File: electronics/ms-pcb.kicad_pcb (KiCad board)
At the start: 2 copper layers, 110 x 110 mm, 28 parts, among them J1 Left motor, J2 Right motor, J3 XT60-M, U1 ESP32-S3-DEVKITC-1U-N8R2, U2 GY-521

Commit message: elec: start PCB v1.1.0
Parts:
- added C1: 0.1uF, Capacitor_THT:CP_Radial_D5.0mm_P2.00mm, F.Cu at (108.7, 107.0)
- added C2: 0.1uF, Capacitor_THT:CP_Radial_D5.0mm_P2.00mm, F.Cu at (141.0, 106.7)
- added D1: D_Schottky, Diode_SMD:D_1206_3216Metric_Pad1.42x1.75mm_HandSolder, F.Cu at (148.8, 76.2)
- added D2: DEBUG, LED_SMD:LED_1206_3216Metric_Pad1.42x1.75mm_HandSolder, F.Cu at (87.4, 76.7)
- added R3: 10k, Resistor_SMD:R_1206_3216Metric_Pad1.30x1.75mm_HandSolder, F.Cu at (130.0, 65.0)
- added R4: 5k, Resistor_SMD:R_1206_3216Metric_Pad1.30x1.75mm_HandSolder, F.Cu at (97.8, 64.8)
- added R8: 1k, Resistor_SMD:R_1206_3216Metric_Pad1.30x1.75mm_HandSolder, F.Cu at (136.9, 65.0)
- D3: renamed from D1; value GREEN -> LED_VBAT
- D4: renamed from D2; value BLUE -> LED_3V3
- H5: renamed from H2; value Caster_wheel_holes -> Caster_wheel
- H6: renamed from H5; value Caster_wheel_holes -> Caster_wheel
- moved U1 2.93 mm to (123.6, 71.0), turned to 90 degrees
- moved D3 2.12 mm to (132.6, 103.8)
- moved R5 2.12 mm to (132.6, 98.8)
- renumbered H3 to H1, H6 to H2, H1 to H3, R3 to R5, R4 to R6, R5 to R7
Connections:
- R2 pad 2: Vmes -> Mes_bat
- R7 pad 1: Vmes -> Mes_bat
- S1 pad G1: Net-(S1-PadG1) -> unconnected-(S1-PadG1)_0
- S1 pad G2: Net-(S1-PadG1) -> unconnected-(S1-PadG1)
- U1 pad J1_10: unconnected-(U1-GPIO17-PadJ1_10) -> button
- U1 pad J1_13: unconnected-(U1-GPIO3-PadJ1_13) -> Mes_bat
- U1 pad J1_14: unconnected-(U1-GPIO46-PadJ1_14) -> DRV_L1
- U1 pad J1_15: unconnected-(U1-GPIO9-PadJ1_15) -> DRV_L2
- U1 pad J1_16: XSHUT_FR -> DRV_R2
- U1 pad J1_17: XSHUT_R -> DRV_R1
- U1 pad J1_19: XSHUT_L -> ENC_R1
- U1 pad J1_20: XSHUT_FL -> ENC_R2
- U1 pad J1_21: +BATT -> Net-(D1-K)
- U1 pad J1_4: SDA -> ENC_L1
- U1 pad J1_5: SCL -> ENC_L2
- U1 pad J1_6: unconnected-(U1-GPIO6-PadJ1_6) -> buzzer
- U1 pad J3_10: DRV_R1 -> unconnected-(U1-GPIO38-PadJ3_10)
- U1 pad J3_11: DRV_R2 -> unconnected-(U1-GPIO37-PadJ3_11)
- U1 pad J3_12: DRV_L2 -> unconnected-(U1-GPIO36-PadJ3_12)
- U1 pad J3_13: DRV_L1 -> unconnected-(U1-GPIO35-PadJ3_13)
- U1 pad J3_16: buzzer -> Mes_VCC
- U1 pad J3_17: button -> SDA
- U1 pad J3_18: ENC_L2 -> SCL
- U1 pad J3_19: Vmes -> XSHUT_FR
- U1 pad J3_20: ENC_L1 -> XSHUT_R
- U1 pad J3_4: unconnected-(U1-GPIO1-PadJ3_4) -> XSHUT_FL
- U1 pad J3_5: unconnected-(U1-GPIO2-PadJ3_5) -> DEBUG
- U1 pad J3_6: ENC_R2 -> unconnected-(U1-MTMS/GPIO42-PadJ3_6)
- U1 pad J3_7: ENC_R1 -> unconnected-(U1-MTDI/GPIO41-PadJ3_7)
- U1 pad J3_8: unconnected-(U1-MTDO/GPIO40-PadJ3_8) -> XSHUT_L
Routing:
- net +BATT: track 193.4 -> 84.4 mm
- net SDA: track 175.3 -> 112.4 mm
- net SCL: track 185.9 -> 123.9 mm
- net Vmes: track 59.5 -> 0.00 mm, vias 1 -> 0
- net XSHUT_R: track 44.0 -> 0.00 mm, vias 2 -> 0
- net XSHUT_FR: track 43.6 -> 0.00 mm, vias 2 -> 0
- net MOT_R2: track 40.2 -> 0.00 mm
- net MOT_R1: track 35.9 -> 0.07 mm
- net MOT_L2: track 34.3 -> 0.00 mm
- net XSHUT_FL: track 34.1 -> 0.00 mm
- net MOT_L1: track 33.3 -> 0.00 mm
- net ENC_L2: track 30.1 -> 3.90 mm
- net XSHUT_F: track 23.4 -> 0.00 mm
- net ENC_L1: track 26.9 -> 4.16 mm
- net +3.3V: track 31.5 -> 11.8 mm, vias 5 -> 3
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
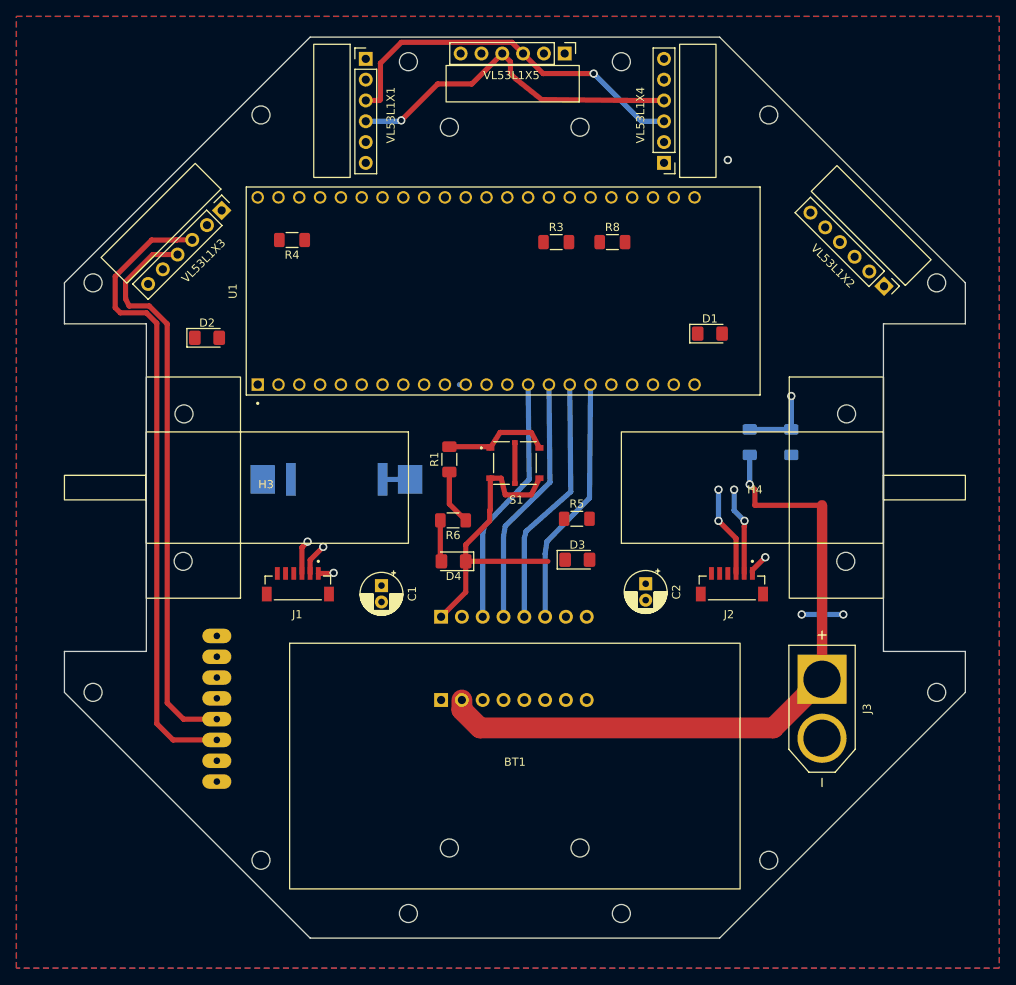
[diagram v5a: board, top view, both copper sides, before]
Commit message: elec: PCB v1.1.0 finished
Still need last checks before ordering.
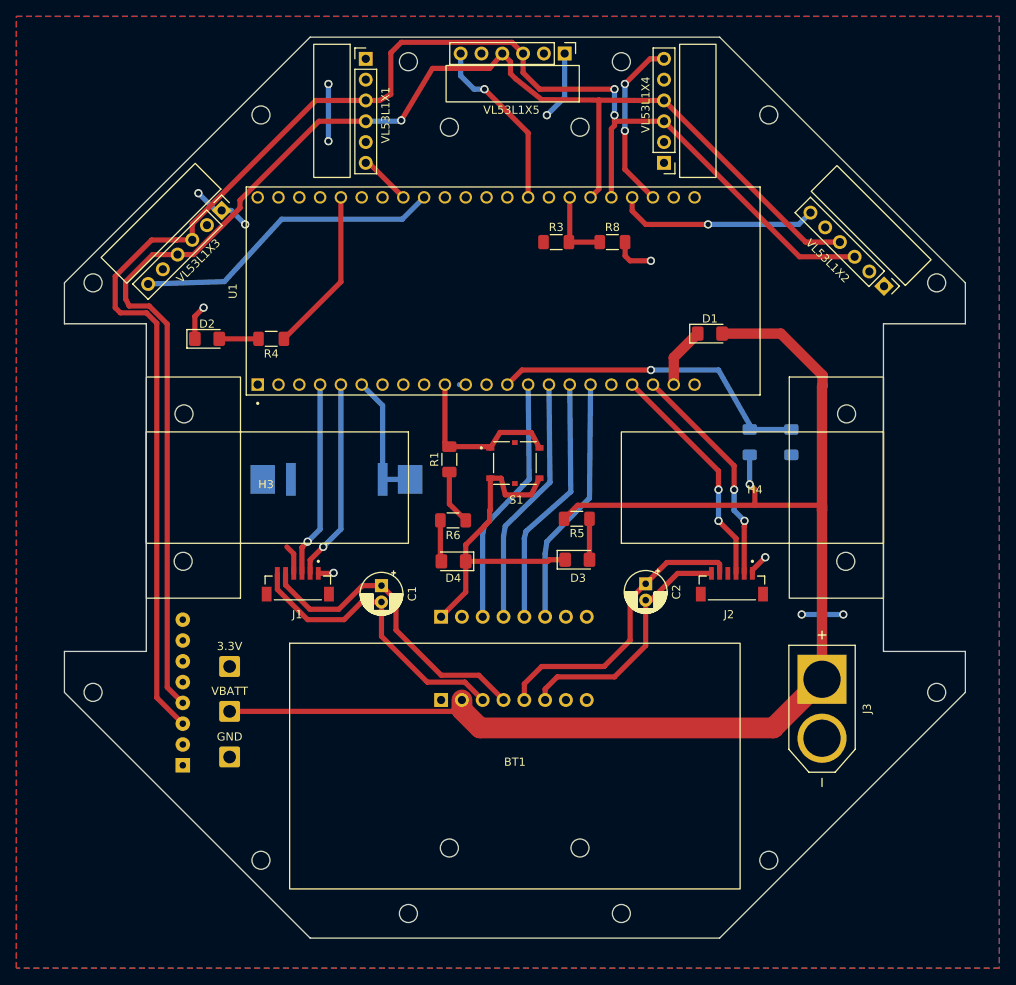
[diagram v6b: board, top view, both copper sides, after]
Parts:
- added 3.3V: Debug_3.3V, Connector_Wire:SolderWire-0.75sqmm_1x01_D1.25mm_OD2.3mm, F.Cu at (90.2, 116.8)
- added GND: Debug_GND, Connector_Wire:SolderWire-0.75sqmm_1x01_D1.25mm_OD2.3mm, F.Cu at (90.2, 127.9)
- added VBATT: Debug_VBAT, Connector_Wire:SolderWire-0.75sqmm_1x01_D1.25mm_OD2.3mm, F.Cu at (90.2, 122.3)
- moved R4 12.3 mm to (95.2, 76.8)
- moved U2 7.23 mm to (90.6, 120.0)
- moved REF** 5.75 mm to (99.7, 71.8)
- moved D2 0.13 mm to (87.4, 76.8)
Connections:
- U1 pad J1_18: XSHUT_F -> unconnected-(U1-GPIO12-PadJ1_18)
- U1 pad J3_14: unconnected-(U1-GPIO0-PadJ3_14) -> XSHUT_F
- U1 pad J3_4: XSHUT_FL -> unconnected-(U1-GPIO1-PadJ3_4)
- U1 pad J3_9: unconnected-(U1-MTCK/GPIO39-PadJ3_9) -> XSHUT_FL
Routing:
- net +BATT: track 84.4 -> 167.7 mm
- net SDA: track 112.4 -> 178.5 mm
- net SCL: track 123.9 -> 190.0 mm, vias 1 -> 2
- net MOT_L2: track 0.00 -> 38.4 mm
- net XSHUT_FL: track 0.00 -> 38.2 mm
- net MOT_L1: track 0.00 -> 37.3 mm
- net MOT_R2: track 0.00 -> 36.2 mm
- net Mes_bat: track 9.16 -> 39.9 mm
- net MOT_R1: track 0.07 -> 30.8 mm
- net +3.3V: track 11.8 -> 38.1 mm, vias 3 -> 7
- net XSHUT_FR: track 0.00 -> 24.7 mm, vias 0 -> 1
- net XSHUT_F: track 0.00 -> 21.7 mm, vias 0 -> 1
- net XSHUT_R: track 0.00 -> 21.3 mm, vias 0 -> 2
- net ENC_L2: track 3.90 -> 24.6 mm
- net DEBUG: track 0.00 -> 20.2 mm
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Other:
- board text added: "Algernon v1.1.0 Open-source micromouse project GitHub: @opatiny"
- board text removed: "Algernon v1.0.0 Open-source micromouse project GitHub: @opatiny"

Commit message: elec: final check for PCB v1.1.0
Refs: #51
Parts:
- added C3: 220uF, Capacitor_SMD:CP_Elec_8x10.5, F.Cu at (160.7, 74.3)
- D3: value LED_VBAT -> VBAT
- D4: value LED_3V3 -> 3V3
- H7: renamed from 3.3V; value Debug_3.3V -> 3V3
- H8: renamed from VBATT; value Debug_VBAT -> VBAT
- H9: renamed from GND; value Debug_GND -> GND
- moved J3 1.40 mm to (162.6, 123.4)
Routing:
- net GND: track 54.8 -> 63.2 mm

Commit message: elec: minor changes in PCB
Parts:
- R4: value 5k -> 30k
- R5: value 40k -> 30k
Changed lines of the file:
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@@
 			)
 		)
-		(property "Description" ""
+		(property "Description" "yellow"
 			(at 0 0 0)
 			(unlocked yes)
@@
 			)
 		)
-		(property "Description" ""
+		(property "Description" "blue"
 			(at 0 0 180)
 			(unlocked yes)
@@
 			)
 		)
-		(property "Value" "5k"
+		(property "Value" "30k"
 			(at 0 1.82 180)
 			(layer "F.Fab")
@@
 			)
 		)
-		(property "Description" ""
+		(property "Description" "green"
 			(at 0 0 0)
 			(unlocked yes)
@@
 			)
 		)
-		(property "Value" "40k"
+		(property "Value" "30k"
 			(at 0 -1.778 0)
 			(layer "F.Fab")
